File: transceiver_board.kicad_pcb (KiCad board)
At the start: 2 copper layers, 212.5 x 77.2 mm, 128 parts, among them J1 85505-5113, J2 Conn_01x01_Male, J3 Laser, J4 Conn_01x01_Male, J5 Receiver Connector, Q1 BC547, Q2 BC547, T1 S558-5999-46-F, U1 LAN83C185-JT, U2 ltc6752ims8-2-pbf, U4 AP63203WU, U5 AP63205WU, U6 LM317_TO-220, U7 LM317_TO-220, Y1 25 MHz

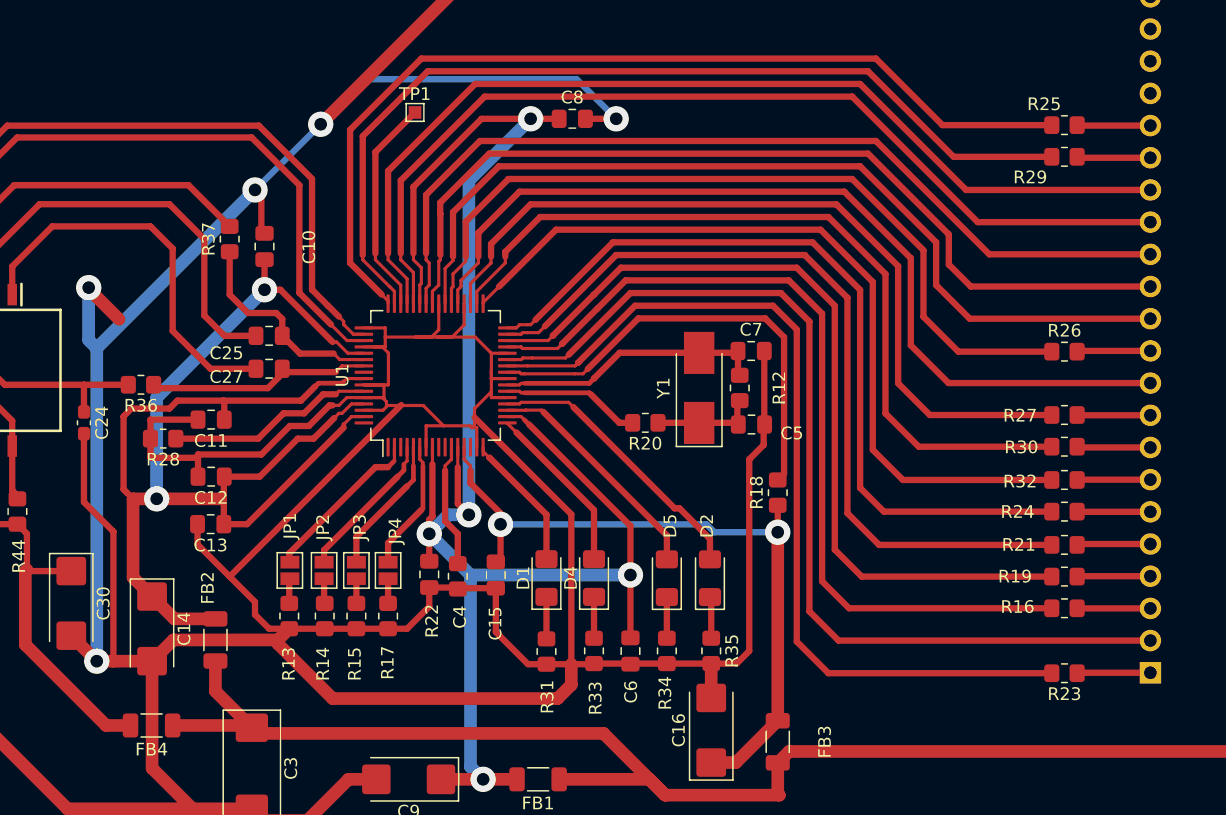
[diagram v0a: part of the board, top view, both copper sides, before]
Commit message: made 2nd rev changes to ethernet side
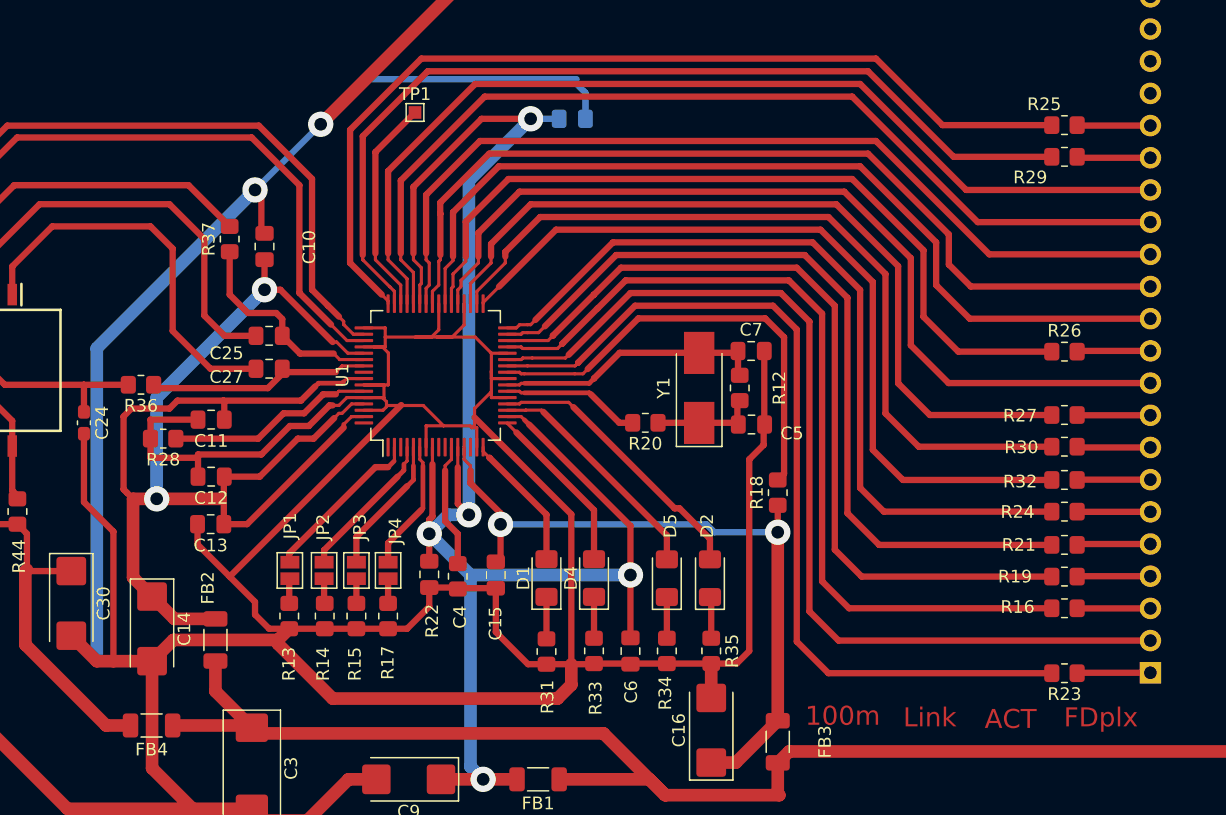
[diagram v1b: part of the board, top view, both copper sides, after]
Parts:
- C8: moved to B.Cu
- R31, R33, R34, R35: value 330R -> 1k
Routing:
- net GND: track 820.6 -> 808.8 mm, vias 7 -> 4
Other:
- board text added: "100m"
- board text added: "ACT"
- board text added: "FDplx"
- board text added: "Link"

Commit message: revised laser driver and power supplies
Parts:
- added D6: 1N4148, Diode_THT:D_DO-35_SOD27_P7.62mm_Horizontal, B.Cu at (205.2, 68.6)
- added D7: 1N4148, Diode_THT:D_DO-35_SOD27_P7.62mm_Horizontal, B.Cu at (205.5, 64.5)
- added R45: 200R, Resistor_THT:R_Axial_DIN0207_L6.3mm_D2.5mm_P10.16mm_Horizontal, B.Cu at (177.0, 55.1)
- added R47: 200R, Resistor_THT:R_Axial_DIN0207_L6.3mm_D2.5mm_P10.16mm_Horizontal, B.Cu at (177.0, 48.5)
- added R48: 200R, Resistor_THT:R_Axial_DIN0207_L6.3mm_D2.5mm_P10.16mm_Horizontal, B.Cu at (177.0, 59.2)
- added R49: 200R, Resistor_THT:R_Axial_DIN0207_L6.3mm_D2.5mm_P10.16mm_Horizontal, B.Cu at (177.0, 44.5)
- C8: moved to F.Cu
- R11, R2, R3, R4: value 240R -> 200R
- moved RV2 19.8 mm to (218.2, 48.0), turned to 0 degrees
- moved R3 19.6 mm to (203.2, 59.2), turned to 0 degrees
- moved R11 19.3 mm to (203.2, 55.1), turned to 0 degrees
- moved RV3 18.1 mm to (198.6, 54.4), turned to 180 degrees
- moved U7 17.7 mm to (198.4, 46.7), turned to 180 degrees
- moved R46 17.6 mm to (222.5, 50.0), turned to 180 degrees
- moved U6 11.7 mm to (218.2, 55.7)
- moved C42 11.3 mm to (222.5, 52.3), turned to 0 degrees
- moved R1 10.4 mm to (194.3, 52.1)
- moved C17 10.3 mm to (225.6, 53.3)
- moved R4 9.13 mm to (203.2, 44.5), turned to 0 degrees
- moved R2 7.45 mm to (203.2, 48.5), turned to 0 degrees
- moved C43 6.33 mm to (190.2, 49.8), turned to -90 degrees
- moved C44 3.33 mm to (194.3, 49.8), turned to 180 degrees
- moved J3 1.50 mm to (211.1, 68.3)
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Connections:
- Q1 pad 1: /laser/High volt -> Net-(R2-Pad1)
- Q1 pad 3: Net-(J3-Pad1) -> GND
- Q2 pad 1: /laser/Low volt -> Net-(Q2-Pad1)
- Q2 pad 3: Net-(J3-Pad1) -> GND
- R11 pad 1: GND -> Net-(R2-Pad1)
- R11 pad 2: /laser/Low volt -> /laser/High volt
- R2 pad 1: GND -> Net-(R2-Pad1)
- R3 pad 1: GND -> Net-(R2-Pad1)
- R3 pad 2: /laser/Low volt -> /laser/High volt
- R4 pad 1: GND -> Net-(R2-Pad1)
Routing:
- net GND: track 808.8 -> 857.0 mm, vias 4 -> 7
- net Net-(Q2-Pad1): track 0.00 -> 37.8 mm
- net Net-(R2-Pad1): track 0.00 -> 30.1 mm
- net Net-(J3-Pad1): track 33.2 -> 10.1 mm
- net +12V: track 139.9 -> 151.4 mm
- net /laser/Low volt: track 20.3 -> 29.9 mm
- net /laser/High volt: track 37.0 -> 30.8 mm
- net Net-(RV3-Pad2): track 7.93 -> 11.1 mm
- net Net-(RV2-Pad2): track 8.43 -> 11.3 mm
- net FPGA_TXn: track 15.1 -> 16.6 mm
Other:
- board text added: "RX"
- board text added: "Revision 3"
- board text added: "TX"
- board text removed: "100m"
- board text removed: "ACT"
- board text removed: "FDplx"
- board text removed: "Link"
- board text removed: "Revision 1"

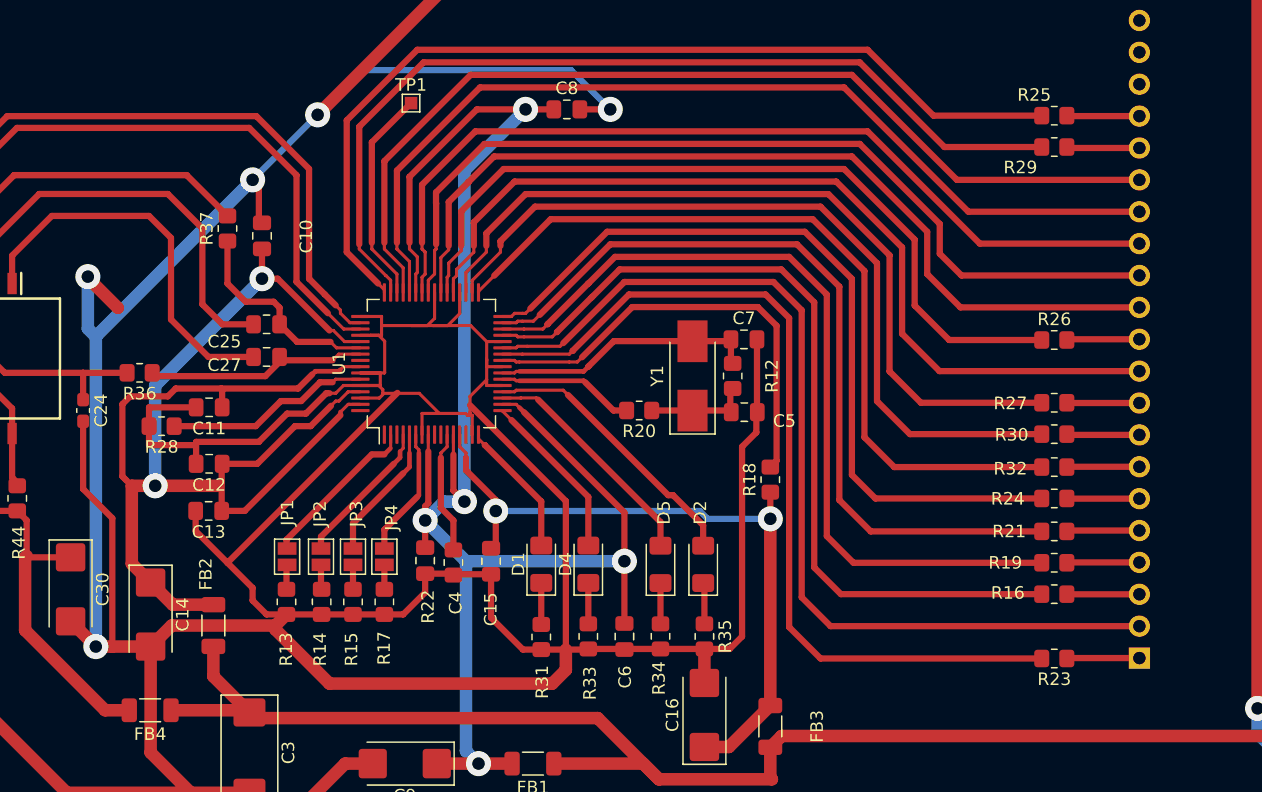
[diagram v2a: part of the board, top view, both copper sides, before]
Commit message: phy side pcb changes that got lost
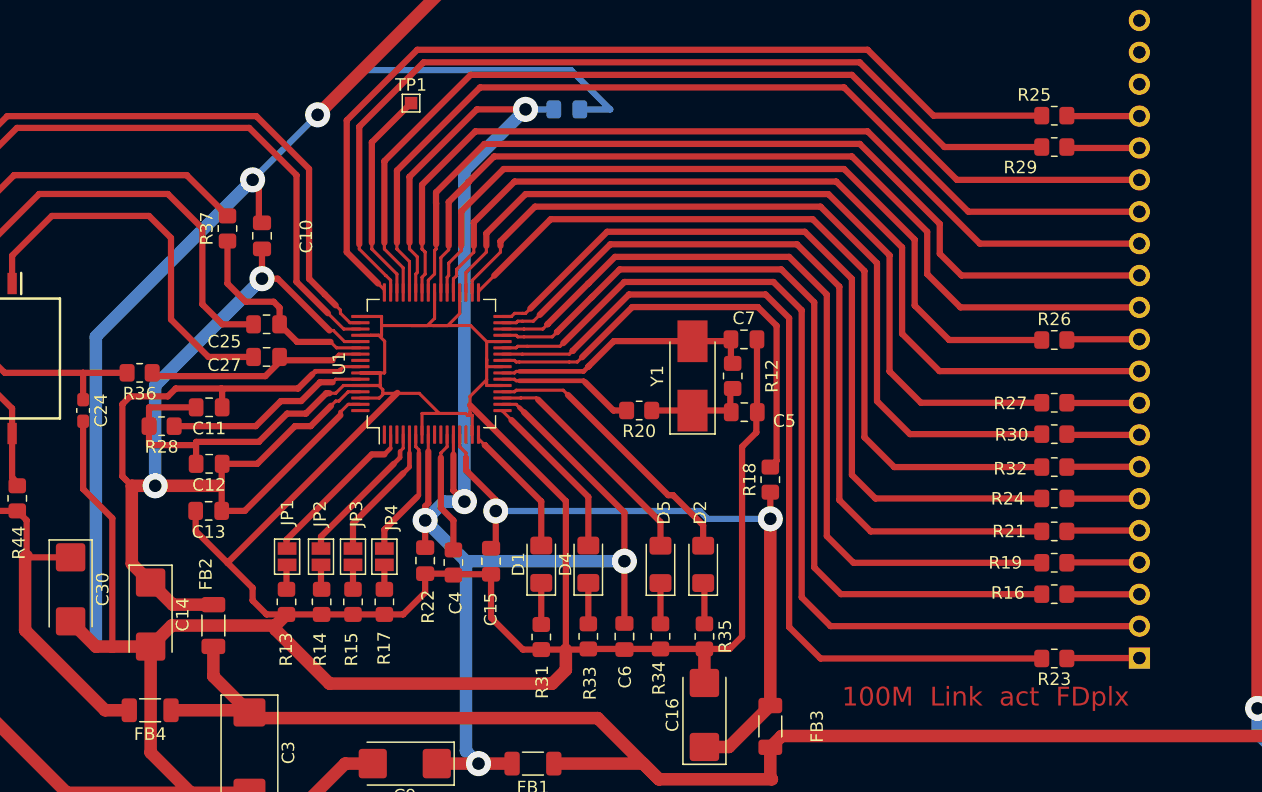
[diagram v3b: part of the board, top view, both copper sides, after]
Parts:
- C8: moved to B.Cu
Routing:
- net GND: track 857.0 -> 848.5 mm, vias 7 -> 4
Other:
- board text added: "100M Link act FDplx"

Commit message: reviewed pcb changes
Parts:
- moved R_L1 7.60 mm to (200.0, 77.5), turned to 90 degrees
- moved C_noise1 6.40 mm to (196.5, 85.0)
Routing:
- net GND: track 848.5 -> 852.8 mm, vias 4 -> 2
- net +5V: track 188.5 -> 191.1 mm
- net Net-(C_noise1-Pad1): track 15.0 -> 16.4 mm

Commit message: fixed mistake
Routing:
- net /laser/Low volt: track 29.9 -> 29.2 mm
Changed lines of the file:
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@@
     (pad_to_mask_clearance 0)
     (pcbplotparams
-      (layerselection 0x0000000_fffffffe)
+      (layerselection 0x0000000_7fffffff)
       (disableapertmacros false)
       (usegerberextensions false)
@@
       (subtractmaskfromsilk false)
       (outputformat 4)
-      (mirror false)
+      (mirror true)
       (drillshape 1)
       (scaleselection 1)
@@
   (segment (start 195.31 52.07) (end 195.31 49.8215) (width 0.508) (layer "F.Cu") (net 26))
   (segment (start 195.3475 49.784) (end 195.3475 47.2225) (width 0.508) (layer "F.Cu") (net 26))
-  (segment (start 195.3475 47.2225) (end 194.861 46.736) (width 0.508) (layer "B.Cu") (net 26))
   (segment (start 181.23525 105.81025) (end 182.39725 106.97225) (width 0.8) (layer "F.Cu") (net 27))
   (segment (start 182.39725 106.97225) (end 183.33325 106.97225) (width 0.8) (layer "F.Cu") (net 27))
